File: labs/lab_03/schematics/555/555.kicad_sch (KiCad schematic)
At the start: 8 parts, among them U1 SE555P

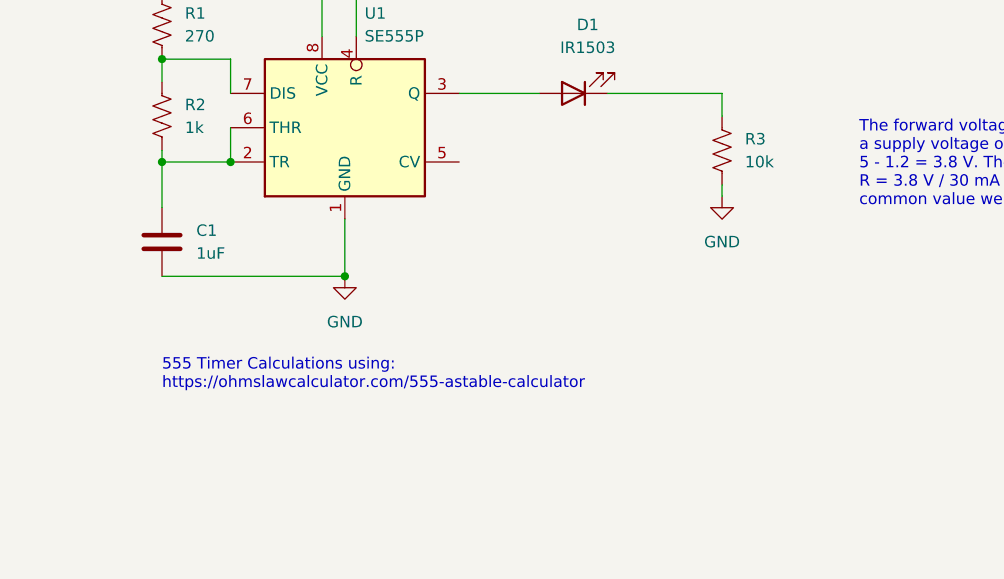
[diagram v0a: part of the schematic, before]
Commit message: Add cap to CV and update comment
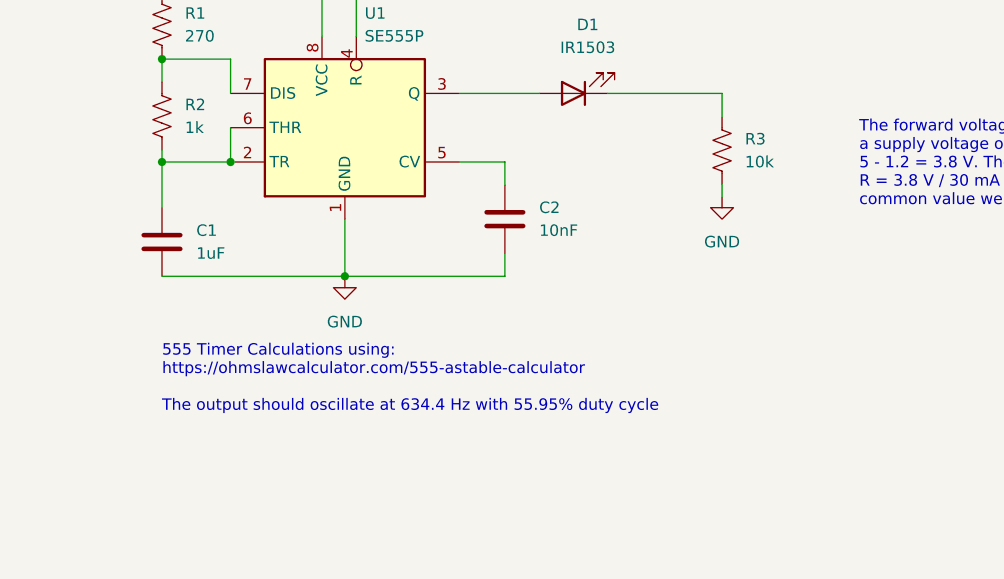
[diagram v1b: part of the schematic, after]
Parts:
- added C2: 10nF, symbol Device:C
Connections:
- net GND: now also C2.2
- net at U1.5 (CV): now also C2.1
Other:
- note added: "555 Timer Calculations using: https://ohmslawcalculator.com/555-astable-calculator The output should oscillate at 634.4 Hz with 55.95% duty cycle"
- note removed: "555 Timer Calculations using: https://ohmslawcalculator.com/555-astable-calculator"
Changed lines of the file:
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@@
     (title "555 Timer & IR LED Driver / Sensor")
     (date "2024-02-05")
-    (rev "1")
+    (rev "2")
     (company "E80 Team 36")
   )
@@
     (stroke (width 0) (type default))
   )
+  (wire (pts (xy 83.82 90.17) (xy 66.04 90.17))
+    (stroke (width 0) (type default))
+  )
   (wire (pts (xy 63.5 57.15) (xy 63.5 63.5))
     (stroke (width 0) (type default))
   )
+  (wire (pts (xy 78.74 77.47) (xy 83.82 77.47))
+    (stroke (width 0) (type default))
+  )
   (wire (pts (xy 78.74 69.85) (xy 87.63 69.85))
     (stroke (width 0) (type default))
@@
     (stroke (width 0) (type default))
   )
+  (wire (pts (xy 83.82 87.63) (xy 83.82 90.17))
+    (stroke (width 0) (type default))
+  )
   (wire (pts (xy 53.34 73.66) (xy 53.34 77.47))
     (stroke (width 0) (type default))
@@
   )
   (wire (pts (xy 45.72 58.42) (xy 45.72 57.15))
+    (stroke (width 0) (type default))
+  )
+  (wire (pts (xy 83.82 77.47) (xy 83.82 80.01))
     (stroke (width 0) (type default))
   )
@@
     (effects (font (size 1.27 1.27)) (justify left bottom))
   )
-  (text "555 Timer Calculations using:\nhttps://ohmslawcalculator.com/555-astable-calculator"
-    (at 45.72 102.87 0)
+  (text "555 Timer Calculations using:\nhttps://ohmslawcalculator.com/555-astable-calculator\n\nThe output should oscillate at 634.4 Hz with 55.95% duty cycle"
+    (at 45.72 105.41 0)
     (effects (font (size 1.27 1.27)) (justify left bottom))
   )
@@
         )
       )
+    )
+  )
+  (symbol (lib_id "Device:C") (at 83.82 83.82 0) (unit 1)
+    (in_bom yes) (on_board yes) (dnp no) (fields_autoplaced)
+    (property "Reference" "C2" (at 87.63 82.55 0)
+      (effects (font (size 1.27 1.27)) (justify left))
+    )
+    (property "Value" "10nF" (at 87.63 85.09 0)
+      (effects (font (size 1.27 1.27)) (justify left))
+    )
+    (property "Footprint" "" (at 84.7852 87.63 0)
+      (effects (font (size 1.27 1.27)) hide)
+    )
+    (property "Datasheet" "~" (at 83.82 83.82 0)
+      (effects (font (size 1.27 1.27)) hide)
+    )
+    (pin "1")
+    (pin "2")
+    (instances
+      (project "555"
+        (path "/35bba517-2448-4f18-9e0f-bb9a81ec92ab"
+          (reference "C2") (unit 1)
+        )
+      )

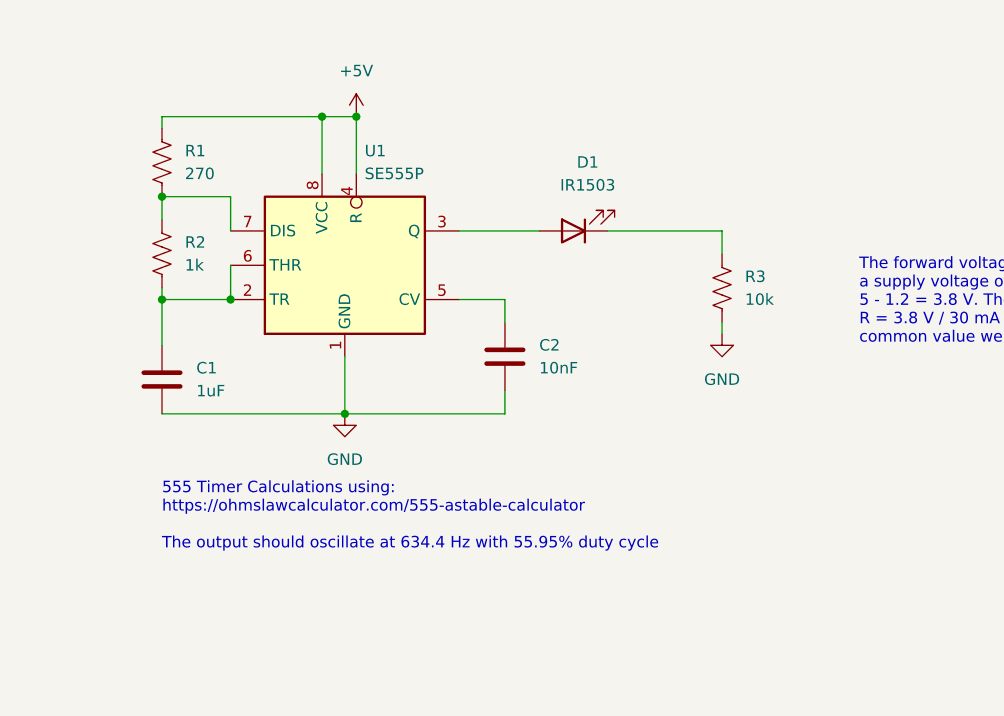
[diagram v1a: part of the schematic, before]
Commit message: Update component values to match lab
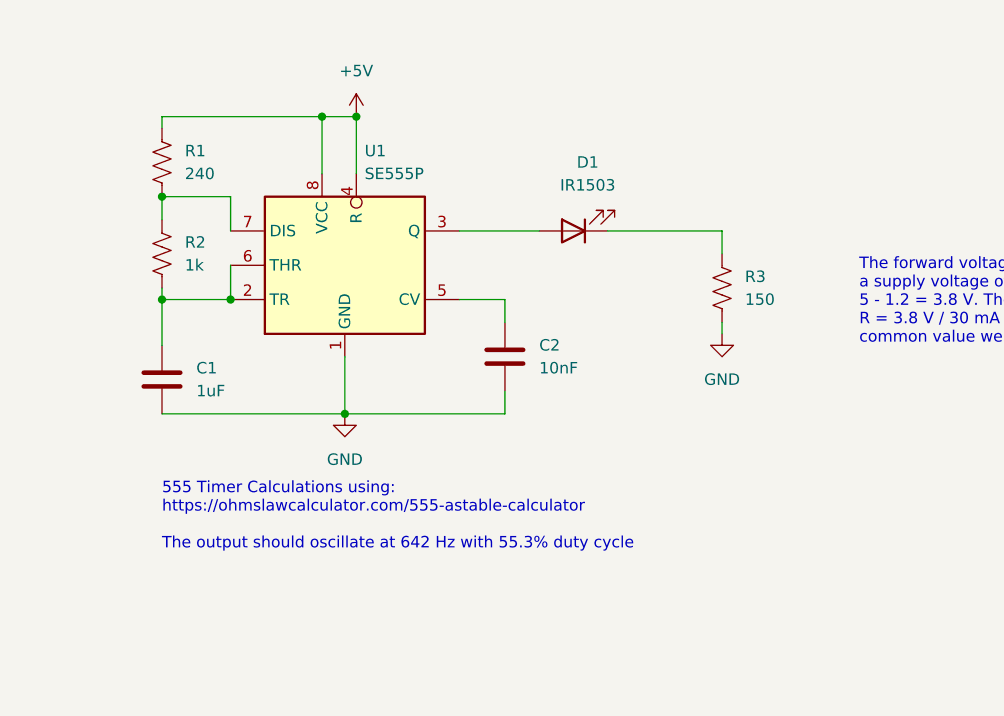
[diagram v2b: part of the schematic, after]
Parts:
- R1: value 270 -> 240
- R3: value 10k -> 150
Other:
- note added: "555 Timer Calculations using: https://ohmslawcalculator.com/555-astable-calculator The output should oscillate at 642 Hz with 55.3% duty cycle"
- note removed: "555 Timer Calculations using: https://ohmslawcalculator.com/555-astable-calculator The output should oscillate at 634.4 Hz with 55.95% duty cycle"
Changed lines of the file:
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@@
     (effects (font (size 1.27 1.27)) (justify left bottom))
   )
-  (text "555 Timer Calculations using:\nhttps://ohmslawcalculator.com/555-astable-calculator\n\nThe output should oscillate at 634.4 Hz with 55.95% duty cycle"
+  (text "555 Timer Calculations using:\nhttps://ohmslawcalculator.com/555-astable-calculator\n\nThe output should oscillate at 642 Hz with 55.3% duty cycle"
     (at 45.72 105.41 0)
     (effects (font (size 1.27 1.27)) (justify left bottom))
@@
       (effects (font (size 1.27 1.27)) (justify left))
     )
-    (property "Value" "270" (at 48.26 63.5 0)
+    (property "Value" "240" (at 48.26 63.5 0)
       (effects (font (size 1.27 1.27)) (justify left))
     )
@@
       (effects (font (size 1.27 1.27)) (justify left))
     )
-    (property "Value" "10k" (at 110.49 77.47 0)
-      (effects (font (size 1.27 1.27)) (justify left))
-    )
+    (property "Value" "150" (at 110.49 77.47 0)
+      (effects (font (size 1.27 1.27)) (justify left))
+    )

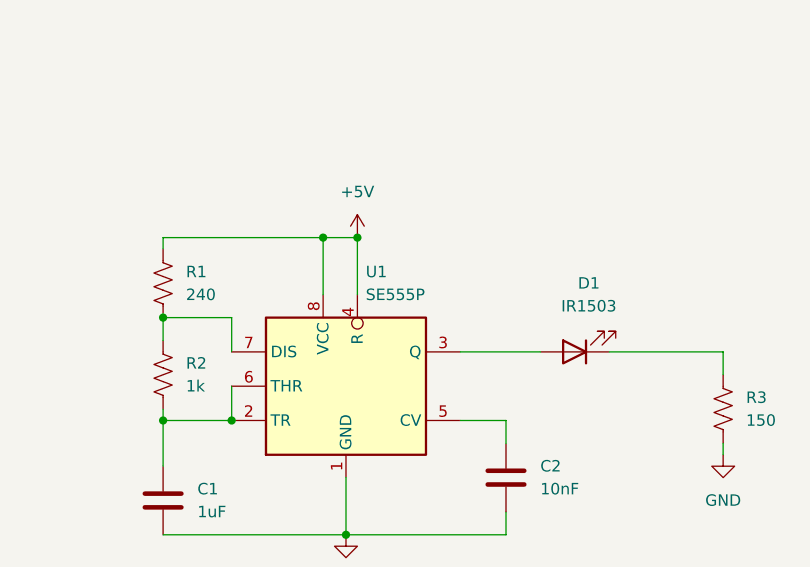
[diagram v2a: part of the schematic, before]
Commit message: Update 555 model number
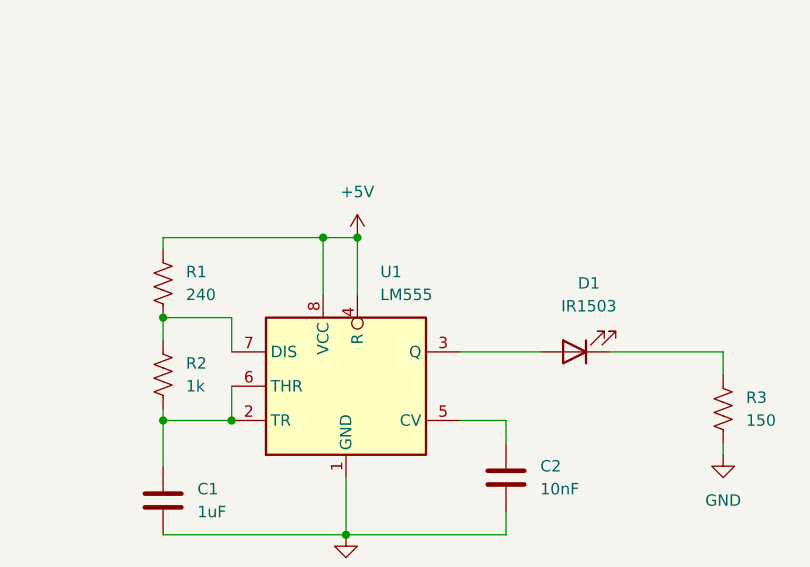
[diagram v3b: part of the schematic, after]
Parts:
- U1: value SE555P -> LM555
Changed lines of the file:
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@@
   )
   (symbol (lib_id "Timer:SE555P") (at 66.04 73.66 0) (unit 1)
-    (in_bom yes) (on_board yes) (dnp no) (fields_autoplaced)
-    (property "Reference" "U1" (at 68.2341 60.96 0)
+    (in_bom yes) (on_board yes) (dnp no)
+    (property "Reference" "U1" (at 69.85 60.96 0)
       (effects (font (size 1.27 1.27)) (justify left))
     )
-    (property "Value" "SE555P" (at 68.2341 63.5 0)
+    (property "Value" "LM555" (at 69.85 63.5 0)
       (effects (font (size 1.27 1.27)) (justify left))
     )
